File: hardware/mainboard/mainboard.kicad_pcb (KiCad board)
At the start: 2 copper layers, 160 x 100 mm, 134 parts, among them M1 JST XH, M2 JST XH, M3 JST XH, M4 JST XH, M5 Micro-Fit 3.0, M6 Micro-Fit 3.0, T1 V_{SA}, T10 TestPoint, T11 TestPoint, T12 TestPoint, T13 TestPoint, T14 TestPoint, T15 TestPoint, T2 Gnd, T3 Clk, T4 SClk, T5 Gnd, T6 MOSI, T7 MISO, T8 V_{CC}IO, T9 TestPoint, U1 STM32F446ZCTx, U2 TMC2208-LA, U3 TMC2208-LA, U4 TMC2208-LA, U5 TMC2208-LA, U6 TMC5160A-TA, U7 TMC5160A-TA

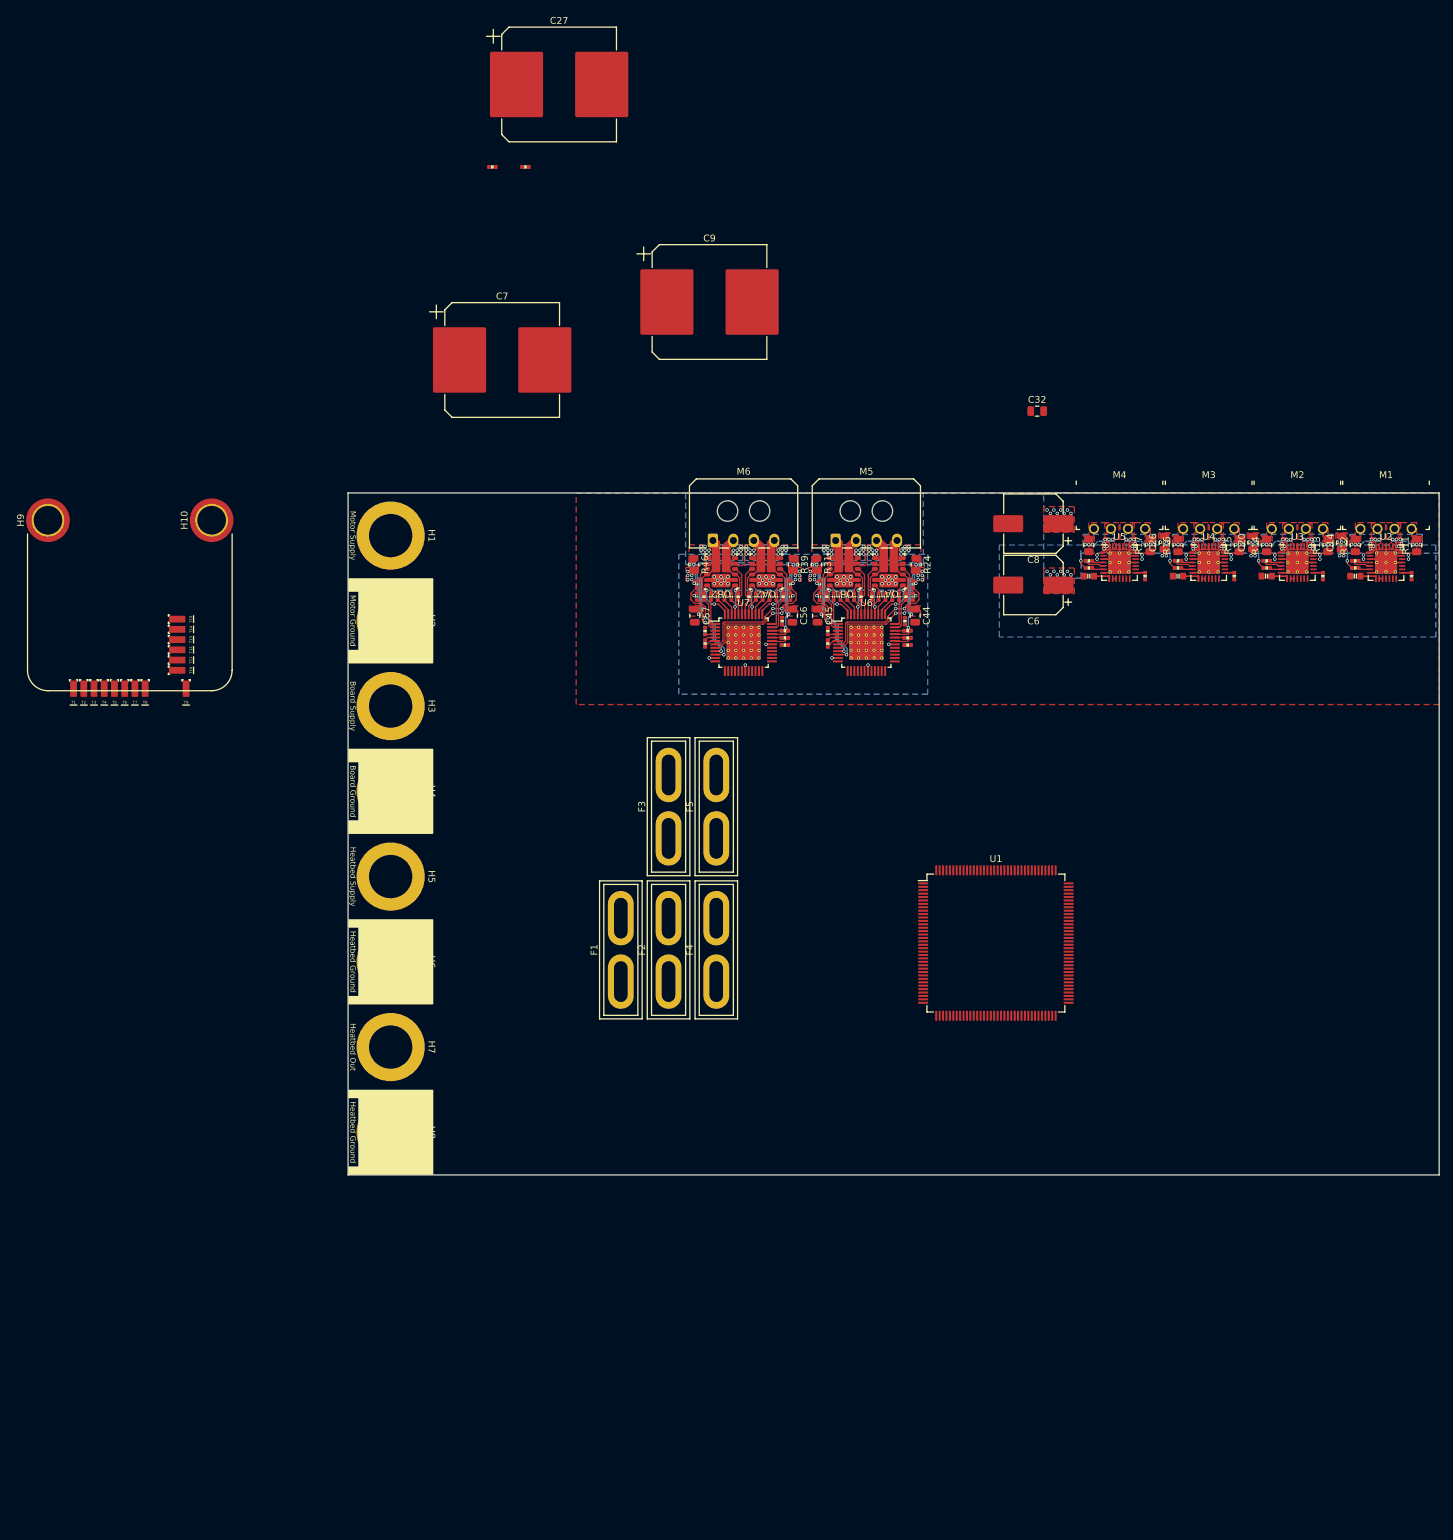
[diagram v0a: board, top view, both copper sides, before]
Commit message: added fan / heater ports to mainboard, and footprints for switches, transistors, etc.
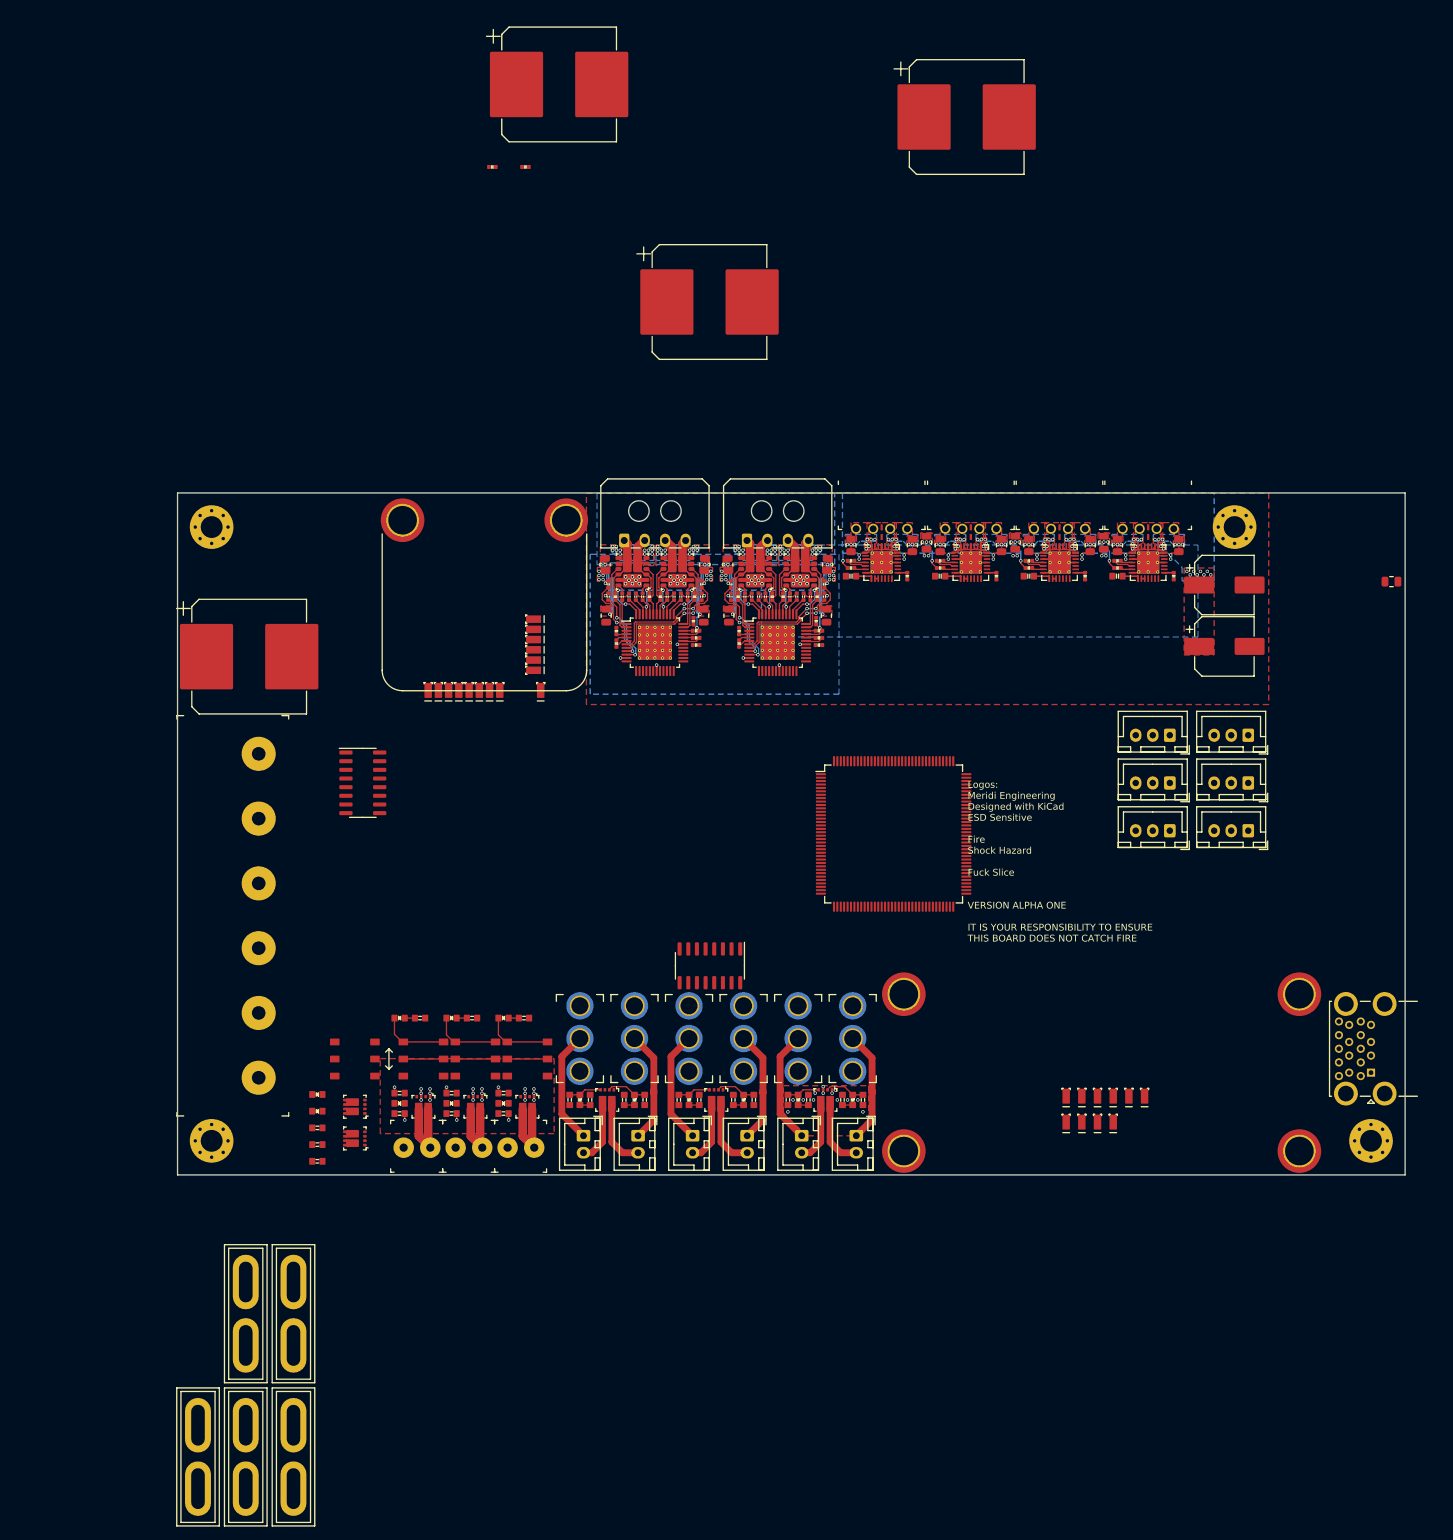
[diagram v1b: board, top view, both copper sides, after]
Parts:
- removed H5: Bed Supply, corevus:M4_PCB_Nut
- removed H6: Gnd, corevus:M4_PCB_Nut
- removed H7: Bed Out, corevus:M4_PCB_Nut
- removed H8: Bed Return, corevus:M4_PCB_Nut
- added C33: 470μF 63V, Capacitor_SMD:CP_Elec_16x17.5, F.Cu at (165.7, -5.12)
- added D10: A, AlphaLib:0603LED, F.Cu at (82.6, 139.5)
- added D12: A, AlphaLib:0603LED, F.Cu at (70.5, 138.2)
- added D13: A, AlphaLib:0603LED, F.Cu at (90.2, 127.0)
- added D14: A, AlphaLib:0603LED, F.Cu at (97.8, 127.0)
- added D15: A, AlphaLib:0603LED, F.Cu at (82.6, 127.0)
- added D18: A, AlphaLib:0603LED, F.Cu at (70.5, 140.7)
- added D2: A, AlphaLib:0603LED, F.Cu at (125.0, 139.0)
- added D3: A, AlphaLib:0603LED, F.Cu at (141.0, 139.0)
- added D4: A, AlphaLib:0603LED, F.Cu at (109.0, 139.0)
- added D5: A, AlphaLib:0603LED, F.Cu at (133.0, 139.0)
- added D6: A, AlphaLib:0603LED, F.Cu at (149.0, 139.0)
- added D7: A, AlphaLib:0603LED, F.Cu at (117.0, 139.0)
- added D8: A, AlphaLib:0603LED, F.Cu at (90.2, 139.5)
- added D9: A, AlphaLib:0603LED, F.Cu at (97.8, 139.5)
- added H11: M2.5, corevus:M3_M2.5_PCB_Nut, F.Cu at (156.5, 123.5)
- added H12: M2.5, corevus:M3_M2.5_PCB_Nut, F.Cu at (156.5, 146.5)
- added H13: M2.5, corevus:M3_M2.5_PCB_Nut, F.Cu at (214.5, 123.5)
- added H14: M2.5, corevus:M3_M2.5_PCB_Nut, F.Cu at (214.5, 146.5)
- added J10: JST XH, Connector_JST:JST_XH_B3B-XH-A_1x03_P2.50mm_Vertical, F.Cu at (207.0, 92.5)
- added J11: JST XH, Connector_JST:JST_XH_B3B-XH-A_1x03_P2.50mm_Vertical, F.Cu at (207.0, 85.5)
- added J12: JST XH, Connector_JST:JST_XH_B2B-XH-A_1x02_P2.50mm_Vertical, F.Cu at (117.5, 144.2)
- added J14: JST XH, Connector_JST:JST_XH_B2B-XH-A_1x02_P2.50mm_Vertical, F.Cu at (125.5, 144.2)
- added J15: JST XH, Connector_JST:JST_XH_B2B-XH-A_1x02_P2.50mm_Vertical, F.Cu at (141.5, 144.2)
- added J16: JST XH, Connector_JST:JST_XH_B2B-XH-A_1x02_P2.50mm_Vertical, F.Cu at (109.5, 144.2)
- added J17: Screw_Terminal_01x02, corevus:DB125-3.81-2P, F.Cu at (92.7, 146.0)
- added J18: Screw_Terminal_01x02, corevus:DB125-3.81-2P, F.Cu at (100.3, 146.0)
- added J19: Screw_Terminal_01x02, corevus:DB125-3.81-2P, F.Cu at (85.1, 146.0)
- added J3: JST XH, Connector_JST:JST_XH_B3B-XH-A_1x03_P2.50mm_Vertical, F.Cu at (195.5, 99.5)
- added J4: JST XH, Connector_JST:JST_XH_B3B-XH-A_1x03_P2.50mm_Vertical, F.Cu at (195.5, 92.5)
- added J5: JST XH, Connector_JST:JST_XH_B3B-XH-A_1x03_P2.50mm_Vertical, F.Cu at (195.5, 85.5)
- added J6: JST XH, Connector_JST:JST_XH_B3B-XH-A_1x03_P2.50mm_Vertical, F.Cu at (207.0, 99.5)
- added J7: JST XH, Connector_JST:JST_XH_B2B-XH-A_1x02_P2.50mm_Vertical, F.Cu at (133.5, 144.2)
- added J8: JST XH, Connector_JST:JST_XH_B2B-XH-A_1x02_P2.50mm_Vertical, F.Cu at (149.5, 144.2)
- added J9: Power Delivery, corevus:DBT50G-9.5-6P, F.Cu at (61.9, 112.0)
- added Q1: AGM308MBP, corevus:AGM308MBP, F.Cu at (145.0, 139.0)
- added Q2: AGM308MBP, corevus:AGM308MBP, F.Cu at (129.0, 139.0)
- added Q3: AGM308MBP, corevus:AGM308MBP, F.Cu at (113.0, 139.0)
- added Q4: AGM308MBP, corevus:AGM308MBP, F.Cu at (101.3, 140.0)
- added Q5: AGM308MBP, corevus:AGM308MBP, F.Cu at (93.7, 140.0)
- added Q6: AGM308MBP, corevus:AGM308MBP, F.Cu at (86.1, 140.0)
- added Q8: AGM308MBP, corevus:AGM308MBP, F.Cu at (76.0, 144.7)
- added Q9: AGM308MBP, corevus:AGM308MBP, F.Cu at (76.0, 140.0)
- added R49: 1kΩ, AlphaLib:0603R, F.Cu at (126.5, 139.0)
- added R50: 1kΩ, AlphaLib:0603R, F.Cu at (90.2, 141.0)
- added R51: 10kΩ, AlphaLib:0603R, F.Cu at (123.5, 139.0)
- added R52: 10kΩ, AlphaLib:0603R, F.Cu at (90.2, 138.0)
- added R53: 1kΩ, AlphaLib:0603R, F.Cu at (142.5, 139.0)
- added R54: 10kΩ, AlphaLib:0603R, F.Cu at (139.5, 139.0)
- added R55: 1kΩ, AlphaLib:0603R, F.Cu at (110.5, 139.0)
- added R56: 10kΩ, AlphaLib:0603R, F.Cu at (107.5, 139.0)
- added R57: 1kΩ, AlphaLib:0603R, F.Cu at (131.5, 139.0)
- added R58: 10kΩ, AlphaLib:0603R, F.Cu at (134.5, 139.0)
- added R59: 1kΩ, AlphaLib:0603R, F.Cu at (147.5, 139.0)
- added R60: 10kΩ, AlphaLib:0603R, F.Cu at (150.5, 139.0)
- added R61: 1kΩ, AlphaLib:0603R, F.Cu at (115.5, 139.0)
- added R62: 10kΩ, AlphaLib:0603R, F.Cu at (118.5, 139.0)
- added R63: 1kΩ, AlphaLib:0603R, F.Cu at (97.8, 141.0)
- added R64: 10kΩ, AlphaLib:0603R, F.Cu at (97.8, 138.0)
- added R65: 1kΩ, AlphaLib:0603R, F.Cu at (82.6, 141.0)
- added R66: 10kΩ, AlphaLib:0603R, F.Cu at (82.6, 138.0)
- added R69: 1kΩ, AlphaLib:0603R, F.Cu at (70.5, 143.1)
- added R70: 1kΩ, AlphaLib:0603R, F.Cu at (93.2, 127.0)
- added R71: 1kΩ, AlphaLib:0603R, F.Cu at (100.8, 127.0)
- added R72: 1kΩ, AlphaLib:0603R, F.Cu at (85.6, 127.0)
- added R76: 1kΩ, AlphaLib:0603R, F.Cu at (70.5, 145.6)
- added R77: 10kΩ, AlphaLib:0603R, F.Cu at (70.5, 148.0)
- added REF**: USB3_A_Molex_48406-0001_Horizontal_Stacked, Connector_USB:USB3_A_Molex_48406-0001_Horizontal_Stacked, F.Cu at (225.0, 135.0)
- added SW10: SW_SPDT, corevus:MST22D18G2-SPST, F.Cu at (93.7, 133.0)
- added SW11: SW_SPDT, corevus:MST22D18G2-SPST, F.Cu at (101.3, 133.0)
- added SW12: SW_SPDT, corevus:MST22D18G2-SPST, F.Cu at (86.1, 133.0)
- added SW3: SPDT, 2A, corevus:SS12D10G4, F.Cu at (149.0, 130.0)
- added SW4: SPDT, 2A, corevus:SS12D10G4, F.Cu at (141.0, 130.0)
- added SW5: SPDT, 2A, corevus:SS12D10G4, F.Cu at (133.0, 130.0)
- added SW6: SPDT, 2A, corevus:SS12D10G4, F.Cu at (125.0, 130.0)
- added SW7: SPDT, 2A, corevus:SS12D10G4, F.Cu at (117.0, 130.0)
- added SW8: SPDT, 2A, corevus:SS12D10G4, F.Cu at (109.0, 130.0)
- added SW9: SW_SPDT, corevus:MST22D18G2-SPST, F.Cu at (76.0, 133.0)
- added T16: 5V, corevus:LGA_Spring, F.Cu at (180.3, 137.9)
- added T17: 5V, corevus:LGA_Spring, F.Cu at (182.6, 137.9)
- added T18: Gnd, corevus:LGA_Spring, F.Cu at (184.9, 137.9)
- added T19: TXD, corevus:LGA_Spring, F.Cu at (187.2, 137.9)
- added T20: RXD, corevus:LGA_Spring, F.Cu at (189.5, 137.9)
- added T21: 5V, corevus:LGA_Spring, F.Cu at (191.8, 137.9)
- added T22: Gnd, corevus:LGA_Spring, F.Cu at (180.3, 141.7)
- added T23: D+, corevus:LGA_Spring, F.Cu at (182.6, 141.7)
- added T24: D-, corevus:LGA_Spring, F.Cu at (184.9, 141.7)
- added T25: Shield, corevus:LGA_Spring, F.Cu at (187.2, 141.7)
- added U8: 4504, Package_SO:SOIC-16_3.9x9.9mm_P1.27mm, F.Cu at (128.1, 119.3)
- added U9: 4504, Package_SO:SOIC-16_3.9x9.9mm_P1.27mm, F.Cu at (77.2, 92.5)
- H1: value VM -> MountingHole; footprint corevus:M4_PCB_Nut -> MountingHole:MountingHole_3.2mm_M3_Pad_Via
- H2, H4: value Gnd -> MountingHole; footprint corevus:M4_PCB_Nut -> MountingHole:MountingHole_3.2mm_M3_Pad_Via
- H3: value Supply -> MountingHole; footprint corevus:M4_PCB_Nut -> MountingHole:MountingHole_3.2mm_M3_Pad_Via
- moved H4 152.6 mm to (225.0, 145.0), turned to 0 degrees
- moved H3 126.5 mm to (205.0, 55.0), turned to 0 degrees
- moved F1 96.8 mm to (53.0, 196.0)
- moved F2 96.8 mm to (60.0, 196.0)
- moved F3 96.8 mm to (60.0, 175.0)
- moved F4 96.8 mm to (67.0, 196.0)
- moved F5 96.8 mm to (67.0, 175.0)
- moved H2 80.6 mm to (55.0, 145.0), turned to 0 degrees
- moved C32 57.7 mm to (228.0, 63.0)
- moved C7 57.2 mm to (60.5, 74.0)
- moved T10 52.0 mm to (101.7, 76.0)
- moved T11 52.0 mm to (101.7, 74.5)
- moved T12 52.0 mm to (101.7, 73.0)
- moved T13 52.0 mm to (101.7, 71.5)
- moved T14 52.0 mm to (101.7, 70.0)
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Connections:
- net Net-(SW1-B) renamed /BOOT0
- C40 pad 1: /Motor 4 (TMCx160)/Motor_A1 -> /Motor 4 (TMCx160)/CA1
- C40 pad 2: /Motor 4 (TMCx160)/CA1 -> /Motor 4 (TMCx160)/Motor_A1
- C41 pad 1: /Motor 4 (TMCx160)/Motor_B1 -> /Motor 4 (TMCx160)/CB1
- C41 pad 2: /Motor 4 (TMCx160)/CB1 -> /Motor 4 (TMCx160)/Motor_B1
- C42 pad 1: /Motor 4 (TMCx160)/CA2 -> /Motor 4 (TMCx160)/Motor_A2
- C42 pad 2: /Motor 4 (TMCx160)/Motor_A2 -> /Motor 4 (TMCx160)/CA2
- C43 pad 1: /Motor 4 (TMCx160)/CB2 -> /Motor 4 (TMCx160)/Motor_B2
- C43 pad 2: /Motor 4 (TMCx160)/Motor_B2 -> /Motor 4 (TMCx160)/CB2
- C52 pad 1: /Motor 5 (TMCx160)/Motor_A1 -> /Motor 5 (TMCx160)/CA1
- C52 pad 2: /Motor 5 (TMCx160)/CA1 -> /Motor 5 (TMCx160)/Motor_A1
- C53 pad 1: /Motor 5 (TMCx160)/Motor_B1 -> /Motor 5 (TMCx160)/CB1
- C53 pad 2: /Motor 5 (TMCx160)/CB1 -> /Motor 5 (TMCx160)/Motor_B1
- C54 pad 1: /Motor 5 (TMCx160)/CA2 -> /Motor 5 (TMCx160)/Motor_A2
- C54 pad 2: /Motor 5 (TMCx160)/Motor_A2 -> /Motor 5 (TMCx160)/CA2
- C55 pad 1: /Motor 5 (TMCx160)/CB2 -> /Motor 5 (TMCx160)/Motor_B2
- C55 pad 2: /Motor 5 (TMCx160)/Motor_B2 -> /Motor 5 (TMCx160)/CB2
- H1 pad 1: unconnected-(H1-Pad1) -> (no net)
- H2 pad 1: GND -> (no net)
- H3 pad 1: +24V -> (no net)
- H4 pad 1: GND -> (no net)
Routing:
- net Net-(J7-Pin_1): track 0.00 -> 16.8 mm
- net Net-(J8-Pin_1): track 0.00 -> 16.8 mm
- net Net-(J12-Pin_1): track 0.00 -> 16.8 mm
- net Net-(J16-Pin_1): track 0.00 -> 16.7 mm
- net Net-(J15-Pin_1): track 0.00 -> 16.7 mm
- net Net-(J14-Pin_1): track 0.00 -> 16.7 mm
- net GND: track 62.9 -> 78.1 mm, vias 56 -> 93
- net Net-(J17-Pin_2): track 0.00 -> 12.1 mm
- net Net-(J19-Pin_2): track 0.00 -> 12.1 mm
- net Net-(J18-Pin_2): track 0.00 -> 12.1 mm
- net Net-(J7-Pin_2): track 0.00 -> 10.3 mm
- net Net-(J8-Pin_2): track 0.00 -> 10.3 mm
- net Net-(J12-Pin_2): track 0.00 -> 10.3 mm
- net /HE0_Gate: track 0.00 -> 10.0 mm
- net /HE2_Gate: track 0.00 -> 9.89 mm
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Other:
- board size 160 x 100 mm -> 180 x 100 mm
- board text added: "Logos: Meridi Engineering Designed with KiCad ESD Sensitive Fire Shock Hazard Fuck Slice VERSION ALPHA ONE IT IS YOUR RESPONSIBILITY TO ENSURE THIS BOARD DOES NOT CATCH FIRE"
- board text removed: "Board Ground"
- board text removed: "Board Supply"
- board text removed: "Heatbed Ground"
- board text removed: "Heatbed Out"
- board text removed: "Heatbed Supply"
- board text removed: "Motor Ground"
- board text removed: "Motor Supply"

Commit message: saving mainboard, gonna tear out the entire thing and redo in 4-layer
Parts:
- removed REF**: USB3_A_Molex_48406-0001_Horizontal_Stacked, Connector_USB:USB3_A_Molex_48406-0001_Horizontal_Stacked
- removed T14, T15: TestPoint, corevus:LGA_Spring
- removed T2: Gnd, corevus:LGA_Spring
- removed T3: Clk, corevus:LGA_Spring
- added C58: 1μF, Capacitor_SMD:C_0805_2012Metric, F.Cu at (85.0, 54.0)
- added C59: 1μF, Capacitor_SMD:C_0805_2012Metric, F.Cu at (77.0, 54.0)
- added C60: 1μF, Capacitor_SMD:C_0805_2012Metric, F.Cu at (87.0, 54.0)
- added C61: 1μF, Capacitor_SMD:C_0805_2012Metric, F.Cu at (79.0, 54.0)
- added C62: 1μF, Capacitor_SMD:C_0805_2012Metric, F.Cu at (89.0, 54.0)
- added C63: 1μF, Capacitor_SMD:C_0805_2012Metric, F.Cu at (91.0, 54.0)
- added C64: 1μF, Capacitor_SMD:C_0805_2012Metric, F.Cu at (81.0, 54.0)
- added C65: 1μF, Capacitor_SMD:C_0805_2012Metric, F.Cu at (83.0, 54.0)
- added D11: A, AlphaLib:0603LED, F.Cu at (80.9, 133.6)
- added D16: A, AlphaLib:0603LED, F.Cu at (80.9, 136.6)
- added D17: P1, AlphaLib:0603LED, F.Cu at (225.5, 120.5)
- added D19: P3, AlphaLib:0603LED, F.Cu at (228.5, 123.5)
- added D20: P2, AlphaLib:0603LED, F.Cu at (228.5, 120.5)
- added D21: P4, AlphaLib:0603LED, F.Cu at (225.5, 123.5)
- added D22: Red, AlphaLib:0603LED, F.Cu at (227.0, 122.0)
- added D23: A, AlphaLib:0603LED, F.Cu at (165.9, 83.2)
- added F6: 10A, corevus:XF-508P-B, F.Cu at (72.0, 123.0)
- added FID1: Fiducial, Fiducial:Fiducial_0.5mm_Mask1mm, F.Cu at (63.2, 57.2)
- added FID2: Fiducial, Fiducial:Fiducial_0.5mm_Mask1mm, F.Cu at (55.0, 131.0)
- added FID3: Fiducial, Fiducial:Fiducial_0.5mm_Mask1mm, F.Cu at (220.0, 145.0)
- added FID4: Fiducial, Fiducial:Fiducial_0.5mm_Mask1mm, F.Cu at (221.0, 57.6)
- added FID5: Fiducial, Fiducial:Fiducial_0.5mm_Mask1mm, F.Cu at (150.0, 91.0)
- added FID6: Fiducial, Fiducial:Fiducial_0.5mm_Mask1mm, F.Cu at (83.5, 114.5)
- added H5: V_{M}, corevus:M3_M2.5_PCB_Nut, F.Cu at (72.0, 54.0)
- added H6: Gnd, corevus:M3_M2.5_PCB_Nut, F.Cu at (96.0, 54.0)
- added J1: USB 2.0, Connector_USB:USB_C_Receptacle_XKB_U262-16XN-4BVC11, F.Cu at (227.5, 93.5)
- added J13: USB_A_Stacked, Connector_USB:USB_A_CUI_UJ2-ADH-TH_Horizontal_Stacked, F.Cu at (224.4, 114.5)
- added J2: Conn_01x05_Pin, Connector_PinHeader_2.54mm:PinHeader_1x05_P2.54mm_Vertical, F.Cu at (161.9, 118.0)
- added J20: Screw_Terminal_01x02, corevus:DB125-3.81-2P, F.Cu at (79.2, 146.3)
- added J21: USB_A_Stacked, Connector_USB:USB_A_CUI_UJ2-ADH-TH_Horizontal_Stacked, F.Cu at (224.4, 136.5)
- added Q10: AGM308MBP, corevus:AGM308MBP, F.Cu at (70.0, 133.4)
- added Q7: AGM308MBP, corevus:AGM308MBP, F.Cu at (81.1, 140.3)
- added R10: 330Ω, AlphaLib:0603R, F.Cu at (224.0, 122.0)
- added R4: 33Ω, AlphaLib:0402R, F.Cu at (221.8, 94.0)
- added R5: 33Ω, AlphaLib:0402R, F.Cu at (221.8, 93.0)
- added R67: 1kΩ, AlphaLib:0603R, F.Cu at (80.9, 131.3)
- added R68: 1kΩ, AlphaLib:0603R, F.Cu at (77.4, 141.6)
- added R73: 10kΩ, AlphaLib:0603R, F.Cu at (77.4, 140.1)
- added R74: 330Ω, AlphaLib:0603R, F.Cu at (222.5, 123.5)
- added R75: 2.7kΩ, AlphaLib:0603R, F.Cu at (215.1, 128.7)
- added R78: 33Ω, AlphaLib:0402R, F.Cu at (219.0, 108.2)
- added R79: 33Ω, AlphaLib:0402R, F.Cu at (219.0, 109.2)
- added R80: 33Ω, AlphaLib:0402R, F.Cu at (219.0, 110.5)
- added R81: 33Ω, AlphaLib:0402R, F.Cu at (219.0, 111.5)
- added R82: 33Ω, AlphaLib:0402R, F.Cu at (219.0, 130.2)
- added R83: 33Ω, AlphaLib:0402R, F.Cu at (219.0, 131.2)
- added R84: 33Ω, AlphaLib:0402R, F.Cu at (219.0, 132.5)
- added R85: 33Ω, AlphaLib:0402R, F.Cu at (219.0, 133.5)
- added R86: 33Ω, AlphaLib:0402R, F.Cu at (205.9, 130.0)
- added R87: 33Ω, AlphaLib:0402R, F.Cu at (205.9, 129.0)
- added R88: 10kΩ, AlphaLib:0603R, F.Cu at (206.0, 132.0)
- added R89: 10kΩ, AlphaLib:0603R, F.Cu at (204.4, 132.0)
- added R9: 330Ω, AlphaLib:0603R, F.Cu at (222.5, 120.5)
- added R90: 1kΩ, AlphaLib:0603R, F.Cu at (165.9, 85.6)
- added SW1: SW_SPDT, corevus:MSS12C02-LS, F.Cu at (77.4, 135.1)
- added SW14: SW_SPDT, corevus:MSS12C02-LS, F.Cu at (156.0, 86.2)
- added T26: TestPoint, corevus:LGA_Spring, F.Cu at (113.8, 76.0)
- added T27: TestPoint, corevus:LGA_Spring, F.Cu at (113.8, 74.5)
- added T28: TestPoint, corevus:LGA_Spring, F.Cu at (113.8, 73.0)
- added T29: TestPoint, corevus:LGA_Spring, F.Cu at (113.8, 71.5)
- added T32: TestPoint, corevus:LGA_Spring, F.Cu at (121.2, 78.2)
- added T33: V_{SA}, corevus:LGA_Spring, F.Cu at (78.8, 78.2)
- added T36: SClk, corevus:LGA_Spring, F.Cu at (80.2, 78.2)
- added T37: Gnd, corevus:LGA_Spring, F.Cu at (81.8, 78.2)
- added T38: MOSI, corevus:LGA_Spring, F.Cu at (83.2, 78.2)
- added T39: MISO, corevus:LGA_Spring, F.Cu at (84.8, 78.2)
- added T40: V_{CC}IO, corevus:LGA_Spring, F.Cu at (86.2, 78.2)
- added T41: TestPoint, corevus:LGA_Spring, F.Cu at (92.2, 78.2)
- added T42: TestPoint, corevus:LGA_Spring, F.Cu at (89.2, 78.2)
- added T43: TestPoint, corevus:LGA_Spring, F.Cu at (81.8, 76.0)
- added T44: TestPoint, corevus:LGA_Spring, F.Cu at (95.8, 76.0)
- added T45: TestPoint, corevus:LGA_Spring, F.Cu at (81.8, 74.5)
- added T46: TestPoint, corevus:LGA_Spring, F.Cu at (95.7, 74.5)
- added T47: TestPoint, corevus:LGA_Spring, F.Cu at (81.8, 73.0)
- added T48: TestPoint, corevus:LGA_Spring, F.Cu at (95.8, 73.0)
- added T49: TestPoint, corevus:LGA_Spring, F.Cu at (81.8, 71.5)
- added T50: TestPoint, corevus:LGA_Spring, F.Cu at (95.8, 71.5)
- added U10: USB2 Hub, Package_SO:SSOP-28_3.9x9.9mm_P0.635mm, F.Cu at (210.2, 133.8)
- added Y2: 12MHz, Crystal:Crystal_SMD_3225-4Pin_3.2x2.5mm, F.Cu at (215.4, 138.4)
- C27, C33, C7, C9: footprint Capacitor_SMD:CP_Elec_16x17.5 -> Capacitor_THT:CP_Radial_D12.5mm_P5.00mm
- F1, F2, F3, F4, F5: footprint Fuse:Fuse_Blade_ATO_directSolder -> corevus:XF-508P-B
- H10, H9: footprint corevus:M3_PCB_Nut -> corevus:M3_M2.5_PCB_Nut
- J9: value Power Delivery -> Power In
- SW10, SW11, SW12, SW9: footprint corevus:MST22D18G2-SPST -> corevus:MSS12C02-LS
- SW3, SW4, SW5, SW6, SW7, SW8: footprint corevus:SS12D10G4 -> corevus:MS-22D28_SPST
- T21: value 5V -> Gnd
- T22: value Gnd -> 5VDet
- moved F2 111.0 mm to (96.0, 91.0), turned to 0 degrees
- moved C33 109.8 mm to (107.0, 87.7), turned to -90 degrees
- moved F4 107.8 mm to (80.0, 89.0), turned to 0 degrees
- moved C15 100.3 mm to (163.0, 77.0)
- moved C27 98.6 mm to (120.0, 87.7), turned to -90 degrees
- moved F1 92.0 mm to (72.0, 106.0), turned to 0 degrees
- moved F3 88.5 mm to (88.0, 91.0), turned to 0 degrees
- moved C21 86.8 mm to (145.0, 77.0)
- moved F5 86.1 mm to (72.0, 89.0), turned to 0 degrees
- moved C9 75.0 mm to (64.8, 62.5), turned to 180 degrees
- moved C32 51.9 mm to (179.0, 46.0)
- moved U1 38.9 mm to (193.8, 103.5)
- moved U9 33.8 mm to (104.0, 113.0)
- moved T22 26.7 mm to (207.0, 143.0), turned to 90 degrees
- moved T10 26.1 mm to (127.8, 76.0)
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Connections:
- net /Motor 4 (TMCx160)/Dir renamed /_{M4}Dir
- net /Motor 4 (TMCx160)/Step renamed /_{M4}Step
- net /Motor 5 (TMCx160)/Dir renamed /_{M5}Dir
- net /Motor 5 (TMCx160)/Step renamed /_{M5}Step
- net /Motor Expansion 1x/_{M0}Dir renamed /_{M10}Dir
- net /Motor Expansion 1x/_{M0}Step renamed /_{M10}Step
- net Net-(D18-A) renamed /BG
- C12 pad 2: VMA -> +24V
- C14 pad 2: VMA -> +24V
- C18 pad 2: VMA -> +24V
- C20 pad 2: VMA -> +24V
- C24 pad 2: VMA -> +24V
- C26 pad 2: VMA -> +24V
- C30 pad 2: VMA -> +24V
- C32 pad 2: VMA -> +24V
- C33 pad 1: VMC -> VMB
- C6 pad 1: VMA -> +24V
- C7 pad 1: VMB -> VMC
- C8 pad 1: VMA -> +24V
- F1 pad 1: +24V -> Net-(J9-Pin_3)
- F1 pad 2: VMA -> +24V
- F3 pad 1: VMB -> +48V
- F3 pad 2: +48V -> VMB
- F5 pad 1: VMC -> +48V
- F5 pad 2: +48V -> VMC
- H9 pad 1: /Motor Expansion 1x/V_{M} -> VMC
- J10 pad 1: +5V -> +3.3V
- J11 pad 1: +5V -> +3.3V
- J3 pad 1: +5V -> +3.3V
- J4 pad 1: +5V -> +3.3V
- J5 pad 1: +5V -> +3.3V
- J6 pad 1: +5V -> +3.3V
- J9 pad 1: GND -> +48V
- J9 pad 2: +48V -> GND
- J9 pad 3: GND -> Net-(J9-Pin_3)
- J9 pad 4: +24V -> GND
- J9 pad 5: /Bed_H- -> /Bed_H+
- J9 pad 6: +24V -> /Bed_H-
- SW10 pad 1: GND -> /HE1_Gate
- SW10 pad 3: /HE1_Gate -> GND
- SW11 pad 1: GND -> /HE0_Gate
- SW11 pad 3: /HE0_Gate -> GND
- SW12 pad 1: GND -> /HE2_Gate
- SW12 pad 3: /HE2_Gate -> GND
- SW9 pad 1: GND -> /Bed_Gate
- SW9 pad 3: /Bed_Gate -> GND
- T1 pad 1: /Motor Expansion 1x/V_{SA} -> +12V
- T21 pad 1: +5V -> GND
- T22 pad 1: GND -> /Raspberry Pi Zero/5VDet
- T23 pad 1: unconnected-(T23-Pad1) -> /Raspberry Pi Zero/DPU
- T24 pad 1: unconnected-(T24-Pad1) -> /Raspberry Pi Zero/DMU
- T4 pad 1: /Motor Expansion 1x/SClk -> /SClk_{1}
- T6 pad 1: /Motor Expansion 1x/MOSI -> /MISO_{1}
- T7 pad 1: /Motor Expansion 1x/MISO -> /MOSI_{1}
- T8 pad 1: /Motor Expansion 1x/V_{CC}IO -> +3.3V
- U1 pad 107: Net-(U1-VSS-Pad107) -> GND
- U1 pad 120: Net-(U1-VSS-Pad107) -> GND
- U1 pad 130: Net-(U1-VSS-Pad107) -> GND
- U1 pad 16: Net-(U1-VSS-Pad107) -> GND
- U1 pad 38: Net-(U1-VSS-Pad107) -> GND
- U1 pad 51: Net-(U1-VSS-Pad107) -> GND
- U1 pad 61: Net-(U1-VSS-Pad107) -> GND
- U1 pad 83: Net-(U1-VSS-Pad107) -> GND
- U1 pad 94: Net-(U1-VSS-Pad107) -> GND
- U2 pad 22: VMA -> +24V
- U2 pad 28: VMA -> +24V
- U3 pad 22: VMA -> +24V
- U3 pad 28: VMA -> +24V
- U4 pad 22: VMA -> +24V
- U4 pad 28: VMA -> +24V
- U5 pad 22: VMA -> +24V
- U5 pad 28: VMA -> +24V
- U6 pad 14: /Motor 4 (TMCx160)/SCK -> /SClk_{1}
- U6 pad 15: /Motor 4 (TMCx160)/SDI -> /MISO_{1}
- U6 pad 16: /Motor 4 (TMCx160)/SDO -> /MOSI_{1}
- U7 pad 14: /Motor 5 (TMCx160)/SCK -> /SClk_{1}
- U7 pad 15: /Motor 5 (TMCx160)/SDI -> /MISO_{1}
- U7 pad 16: /Motor 5 (TMCx160)/SDO -> /MOSI_{1}
- U9 pad 10: unconnected-(U9-Dout-Pad10) -> /HE3_Gate
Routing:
- net GND: track 78.1 -> 177.1 mm, vias 93 -> 265
- net +12V: track 4.02 -> 65.5 mm, vias 0 -> 50
- net +3.3V: track 7.55 -> 65.2 mm, vias 0 -> 2
- net /SClk_{1}: track 0.00 -> 56.1 mm, vias 0 -> 2
- net /MOSI_{1}: track 0.00 -> 52.9 mm, vias 0 -> 2
- net /MISO_{1}: track 0.00 -> 52.3 mm, vias 0 -> 2
- net /Motor Expansion 2x/_{M2}~{EN}: track 0.00 -> 51.5 mm
- net /_{M22}Dir: track 0.00 -> 50.7 mm
- net /_{M22}Step: track 0.00 -> 49.6 mm
- net /Motor Expansion 2x/_{M2}~{CS}: track 0.00 -> 40.9 mm
- net /Motor Expansion 2x/_{M0}~{EN}: track 0.00 -> 38.9 mm
- net Net-(D17-A): track 0.00 -> 38.8 mm, vias 0 -> 2
- net /Motor Expansion 2x/_{M0}~{CS}: track 0.00 -> 37.9 mm
- net /_{M20}Dir: track 0.00 -> 37.6 mm
- net /_{M20}Step: track 0.00 -> 36.4 mm
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- added copper zone on B.Cu, net +12V
- added copper zone on F.Cu, net +12V
- added copper zone on B.Cu, net +24V
- added copper zone on F.Cu, net +24V
- added copper zone on F.Cu, net +48V
- added copper zone on F.Cu, net /Bed_H+
- added copper zone on F.Cu, net /Bed_H-
- added copper zone on F.Cu, net Net-(J17-Pin_2)
- added copper zone on F.Cu, net Net-(J18-Pin_2)
- added copper zone on F.Cu, net Net-(J19-Pin_2)
- added copper zone on F.Cu, net Net-(J20-Pin_2)
- added copper zone on F.Cu, net Net-(J9-Pin_3)
- added copper zone on F.Cu, net VMC
- removed copper zone on B.Cu, net VMA
- removed copper zone on F.Cu, net VMA
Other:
- board text added: "+ HEATBED -"
- board text added: "+ MAIN POWER -"
- board text added: "+ MOTOR POWER -"
- board text added: "12"
- board text added: "12V"
- board text added: "24"
- board text added: "24V"
- board text added: "5V"
- board text added: "DFU"
- board text added: "EN"
- board text added: "Endstops"
- board text added: "FANS"
- board text added: "HEATERS"
- board text added: "High Power Motors"
- board text added: "Low Power Motors"
- board text added: "M0"
- board text added: "M1"
- board text added: "M10"
- board text added: "M12"
- board text added: "M2"
- board text added: "M20"
- board text added: "M22"
- board text added: "M3"
- board text added: "M4"
- board text added: "M5"
- board text added: "MCU"
- board text added: "Motor Expander Sockets"
- board text added: "O"
- board text added: "Power In"
- board text added: "RPi Zero Dock"
- board text added: "Thermistors"
- board text added: "Voltage Selection Fuses"
- board text added: "X"
